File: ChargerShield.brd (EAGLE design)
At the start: 68.6 x 53.3 mm, 26 parts, among them IC1 LM358N, Q1 BD648, Q2 BD648, T2 BC548, X1 +5V, X2 Battery, X3 VCC

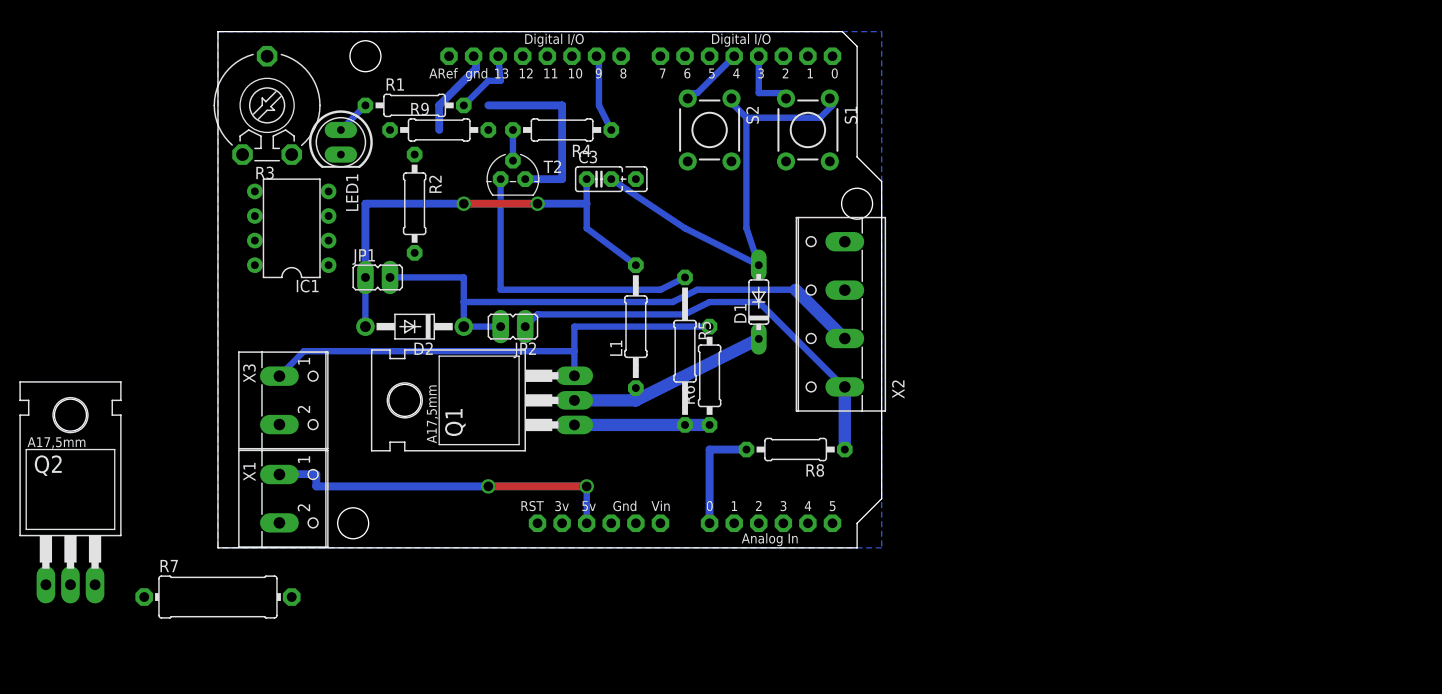
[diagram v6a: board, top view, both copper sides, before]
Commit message: longer Arduino shield
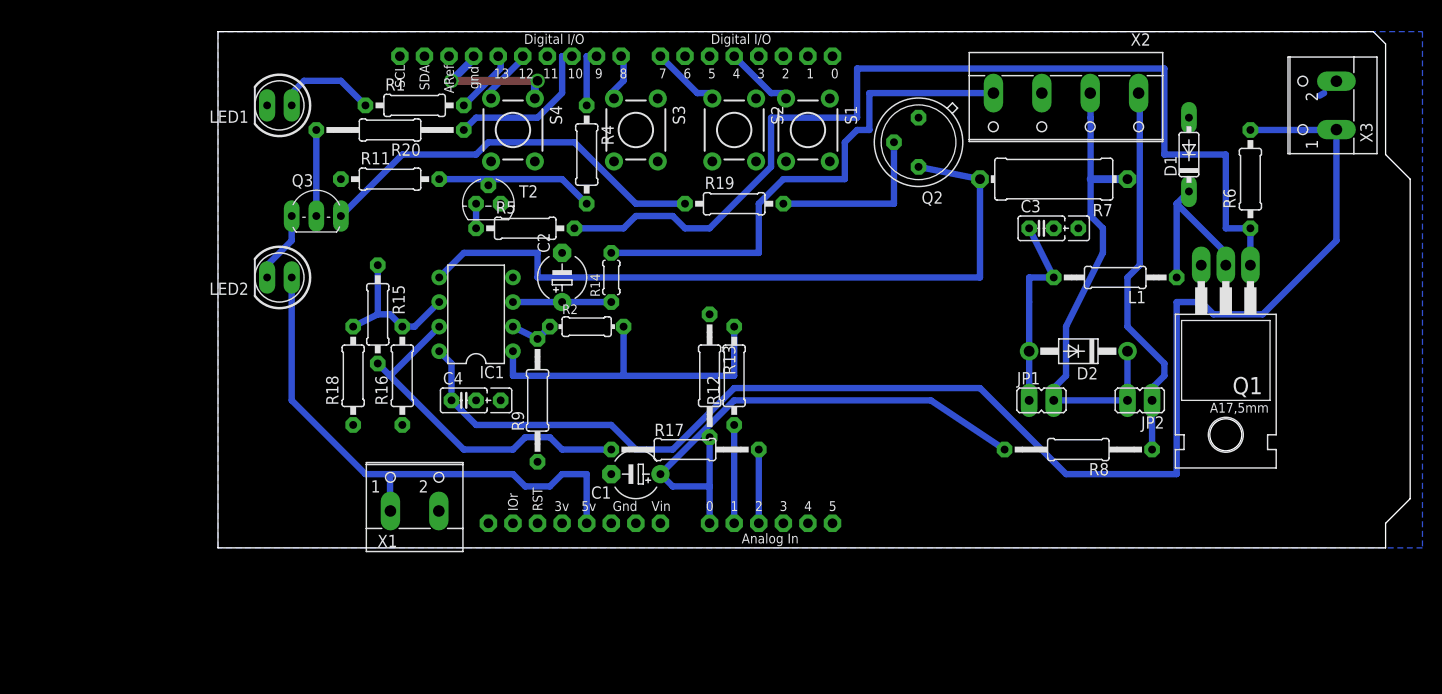
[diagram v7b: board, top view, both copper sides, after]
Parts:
- removed R3: 10k, pot:LI10
- added C1: 10µ, rcl:E5-5
- added C2: 3µ3, rcl:E5-5
- added C4: 100n, rcl:C025_050-025X075
- added LED2: (no value), bigger:LED5MM_BIG
- added Q3: BC548, transistor-npn:TO92-EBC
- added R11, R15: 100k, rcl:0207/10
- added R12: 1k, rcl:0207/10
- added R13: 100k, rcl:0207/12
- added R14: 1k, rcl:0204/5
- added R16: 33k, rcl:0207/10
- added R17, R20: 1k, rcl:0207/15
- added R18: 12k, rcl:0207/10
- added R19: 200, rcl:0207/10
- added S3: Start, SparkFun-Electromechanical:TACTILE-PTH
- added S4: Discharge, SparkFun-Electromechanical:TACTILE-PTH
- Q2: value BD648 -> BC140-10; device transistor-pnp:TO220 -> transistor-npn:TO39
- R2: device rcl:0207/10 -> rcl:0204/7
- R5: device rcl:0207/15 -> rcl:0207/10
- R7: value 1 -> 1R666
- R8: device rcl:0207/10 -> rcl:0207/15
- R9: value 1k -> 10k; device rcl:0207/10 -> rcl:0207/12
- S2: value UP -> Up
- U$1: value ARDUINOUNO -> ARDUINOR3BPLACE-LONG; device adafruit:ARDUINO -> arduino-long:ARDUINOR3-BPLACE-LONG
- moved X3 110.9 mm to (114.3, 45.7), turned to 90 degrees
- moved R7 96.6 mm to (86.4, 38.1), turned to 180 degrees
- moved Q2 96.1 mm to (72.4, 41.9), turned to 180 degrees
- moved Q1 74.1 mm to (104.1, 22.9), turned to 180 degrees
- moved JP1 69.7 mm to (85.1, 15.2)
- moved D2 68.6 mm to (88.9, 20.3)
- moved JP2 65.2 mm to (95.2, 15.2)
- moved R6 59.5 mm to (106.7, 38.1)
- moved L1 49.8 mm to (92.7, 27.9), turned to 180 degrees
- moved D1 47.0 mm to (100.3, 40.6)
- moved C3 46.0 mm to (85.1, 33.0)
- moved X2 32.4 mm to (87.6, 45.7), turned to 180 degrees
- moved R9 29.7 mm to (33.0, 15.2), turned to 90 degrees
- moved R8 29.2 mm to (88.9, 10.2)
- moved R2 21.8 mm to (38.1, 22.9), turned to 0 degrees
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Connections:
- removed net GND1: U$1.GND1
- removed net GND2: U$1.GND2
- removed net U_BATT: R8.2, U$1.A0
- removed net V+: IC1.8
- removed net V-: IC1.4
- new net DISC_1: Q3.E, R19.1
- new net I_BATT1: R12.1, U$1.A1
- new net I_DISC1: R17.2, U$1.A2
- new net N$16: IC1.6, R15.1, R16.2, R18.2
- new net N$17: IC1.7, R15.2, R17.1
- new net N$18: Q2.2, R19.2
- new net N$20: Q3.B, R20.2
- new net N$21: LED2.K, Q3.C
- new net N$22: S3.3, U$1.D8
- new net N$23: S4.3, U$1.D12
- new net N$24: R20.1, U$1.D10
- new net U_BATT1: C1.+, R13.2, R8.2, U$1.A0
- net +5V: now also LED2.A
- net GND: now also C1.-, C2.-, C4.2, IC1.4, Q2.1, R11.1, R13.1, R16.1, R18.1, R9.1, S3.1, S4.1, U$1.GND1, U$1.GND2; no longer R3.A, R7.1
- net I_SENSE: now also R14.2; no longer IC1.3
- net N$11: now also R12.2
- net N$12: now also IC1.5, Q2.3; no longer Q2.2
- net N$13: now also R7.1; no longer Q2.3
- net N$15: now also C2.+, IC1.3, R14.1; no longer R3.E, R3.S, R9.1
- net N$3: now also U$1.D4; no longer U$1.D3
- net N$4: now also U$1.D7; no longer U$1.D4
- net N$5: now also R11.2
- net VCC: now also C4.1, IC1.8
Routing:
- net VCC: track 50.6 -> 151.1 mm
- net N$7: track 14.0 -> 104.0 mm
- net N$12: track 0.00 -> 76.1 mm
- net GND: track 74.4 -> 15.4 mm, vias 0 -> 2
- net U_BATT1: track 0.00 -> 54.8 mm
- net I_SENSE: track 0.00 -> 53.8 mm
- net DISC_1: track 0.00 -> 41.3 mm
- net N$17: track 0.00 -> 36.0 mm
- net N$11: track 0.00 -> 35.6 mm
- net N$6: track 30.8 -> 2.54 mm
- net N$10: track 47.0 -> 20.9 mm, vias 2 -> 0
- net +5V: track 36.9 -> 56.3 mm, vias 2 -> 0
- net N$18: track 0.00 -> 17.8 mm
- net N$24: track 0.00 -> 16.8 mm
- net N$16: track 0.00 -> 15.8 mm
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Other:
- board size 68.6 x 53.3 mm -> 123.2 x 53.3 mm

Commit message: LM324
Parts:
- IC1: value LM358N -> LM324N; device linear:DIL08 -> linear:DIL14
- R14: device rcl:0204/5 -> rcl:0207/10
- R8: device rcl:0207/15 -> rcl:0207/10
- R9: device rcl:0207/12 -> rcl:0207/10
- moved R18 27.4 mm to (40.6, 24.1), turned to 180 degrees
- moved R15 24.7 mm to (40.6, 29.2), turned to 0 degrees
- moved R16 23.3 mm to (40.6, 26.7), turned to 180 degrees
- moved C2 15.3 mm to (45.7, 16.5), turned to 270 degrees
- moved R17 12.7 mm to (55.9, 20.3), turned to 270 degrees
- moved T2 11.7 mm to (16.5, 33.0), turned to 270 degrees
- moved R14 8.03 mm to (48.3, 25.4)
- moved R5 6.84 mm to (25.4, 35.6)
- moved R2 4.02 mm to (39.4, 19.1)
- moved C4 2.84 mm to (26.7, 12.7), turned to 180 degrees
- moved R8 2.54 mm to (86.4, 10.2)
- moved R4 2.54 mm to (38.1, 43.2)
- moved R12 1.27 mm to (53.3, 16.5)
- moved R9 1.27 mm to (33.0, 14.0)
- moved R19 1.27 mm to (53.3, 36.8)
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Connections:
- net GND: now also IC1.11; no longer IC1.4
- net VCC: now also IC1.4; no longer IC1.8
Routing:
- net N$7: track 104.0 -> 115.1 mm
- net N$15: track 10.2 -> 20.6 mm
- net N$17: track 36.0 -> 28.3 mm
- net N$5: track 16.9 -> 24.3 mm
- net N$11: track 35.6 -> 28.7 mm
- net I_SENSE: track 53.8 -> 47.6 mm
- net N$16: track 15.8 -> 10.5 mm
- net N$8: track 39.6 -> 44.7 mm
- net I_DISC1: track 7.62 -> 10.2 mm
- net N$12: track 76.1 -> 73.7 mm
- net PWM: track 6.35 -> 4.08 mm
- net N$6: track 2.54 -> 4.34 mm
- net +5V: track 56.3 -> 54.5 mm
- net VCC: track 151.1 -> 152.7 mm
- net N$13: track 50.2 -> 48.9 mm
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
